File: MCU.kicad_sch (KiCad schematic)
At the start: 104 parts, among them J1 Conn_01x02_Pin, J11 Logger Connector, J12 UART Connector, J13 External UART, J14 External I2C, J15 JTAG Header, J2 Conn_01x02_Pin, J27 Conn_01x02_Pin, SW1 XRSn_button, U13 M24M01E-FMN6TP, U17 TRS3221EIPWR, U18 BZX84C3V3TS-7-F, U19 BZX84C3V3TS-7-F, U20 BZX84C3V3TS-7-F, U21 MIC920YC5-TR, U5 F280025PNS, Y2 H130B-16.000-18-3030-EXT-TR

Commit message: DONE! Added ESD protection & finalized everything before, this thing is ready for production
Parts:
- removed TP63, TP64, TP65, TP66: RCT-0C, digikey-footprints:PROBE_PAD_0805, symbol dk_Test-Points:RCT-0C
- added D10, D9: ESD8104MUTAG, ESD8104MUTAG:DIO_ESD8104MUTAG, symbol ESD8104MUTAG:ESD8104MUTAG
- added U22, U23: ESD7C3.3DT5G, SOT_C3.3DT5G_ONS, symbol ESD7C3-3DT5G:ESD7C3.3DT5G
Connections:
- net GND: now also D10.3 (GND), D10.8 (GND), D9.3 (GND), D9.8 (GND), U22.3, U23.3
- net I2CB_SCL: now also D10.4
- net I2CB_SDA: now also D10.5
- net JTAG_TCK: now also D9.5
- net JTAG_TDI: now also D9.1
- net JTAG_TDO: now also D9.4
- net JTAG_TMS: now also D9.2
- net LINB_RX: now also U23.2
- net LINB_TX: now also U23.1
- net MCU_IO_3V3: now also D10.2
- net RS232_RX: now also U22.1
- net RS232_TX: now also U22.2
- net XRSn: now also D10.1
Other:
- moved on the sheet: C111, C49, C50, C51, C52, C53, C54, C55, C56, C58, C59, C61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

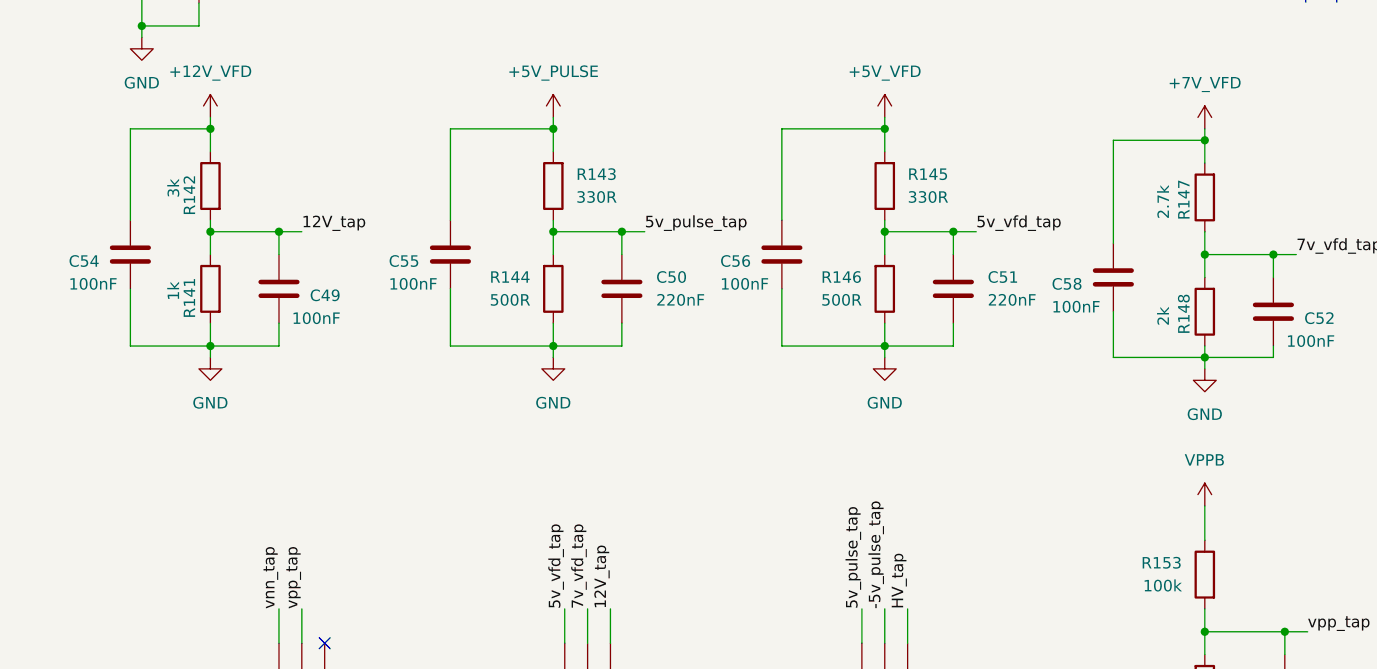
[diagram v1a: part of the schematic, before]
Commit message: edited voltage sensing resistor values to give headroom
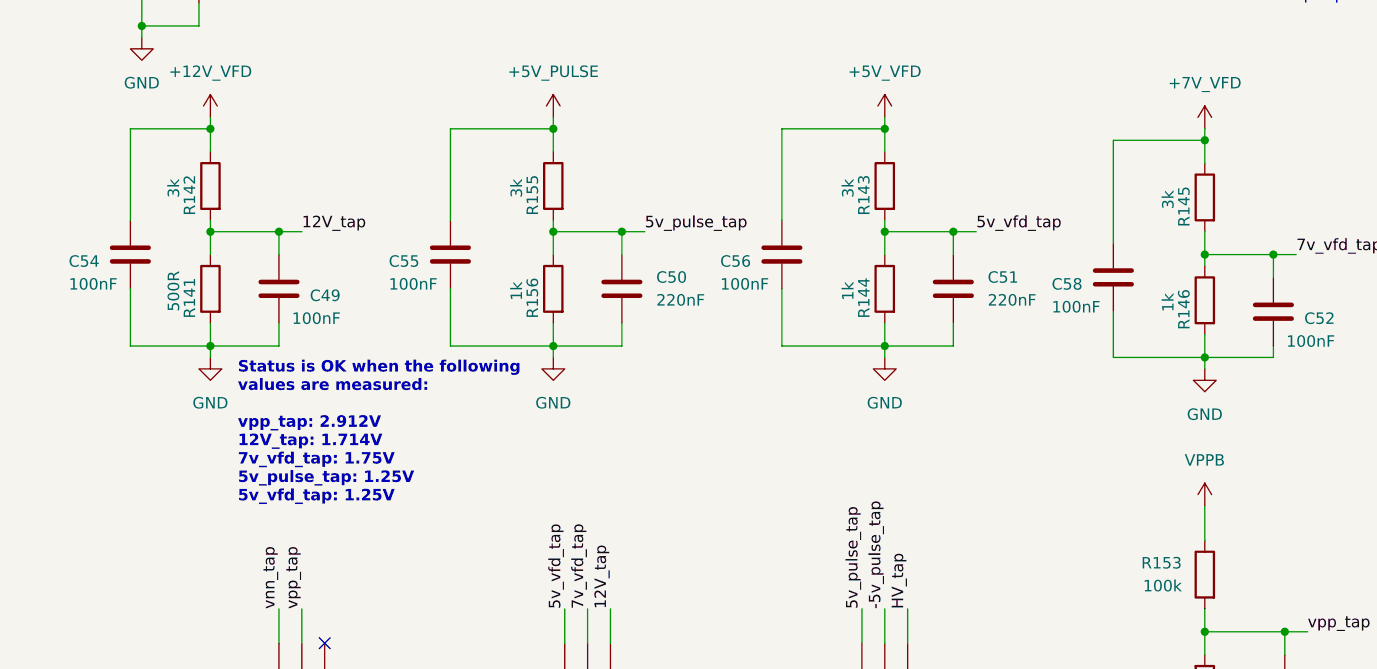
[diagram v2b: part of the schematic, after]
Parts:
- removed R147: 2.7k, Resistor_SMD:R_0603_1608Metric, symbol Device:R
- removed R148: 2k, Resistor_SMD:R_0603_1608Metric, symbol Device:R
- added R155: 3k, Resistor_SMD:R_0603_1608Metric, symbol Device:R
- added R156: 1k, Resistor_SMD:R_0603_1608Metric, symbol Device:R
- R141: value 1k -> 500R
- R143, R145: value 330R -> 3k
- R144, R146: value 500R -> 1k
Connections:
- net +5V_PULSE: now also R155.1; no longer R143.2
- net +5V_VFD: now also R143.1; no longer R145.2
- net +7V_VFD: now also R145.1
- net 5v_pulse_tap: now also R155.2, R156.1; no longer R143.1, R144.2
- net 5v_vfd_tap: now also R143.2, R144.1; no longer R145.1, R146.2
- net 7v_vfd_tap: now also R145.2, R146.1
- net GND: now also R144.2, R146.2, R156.2; no longer R144.1, R146.1
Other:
- note added: "Status is OK when the following values are measured: vpp_tap: 2.912V 12V_tap: 1.714V 7v_vfd_tap: 1.75V 5v_pulse_tap: 1.25V 5v_vfd_tap: 1.25V"

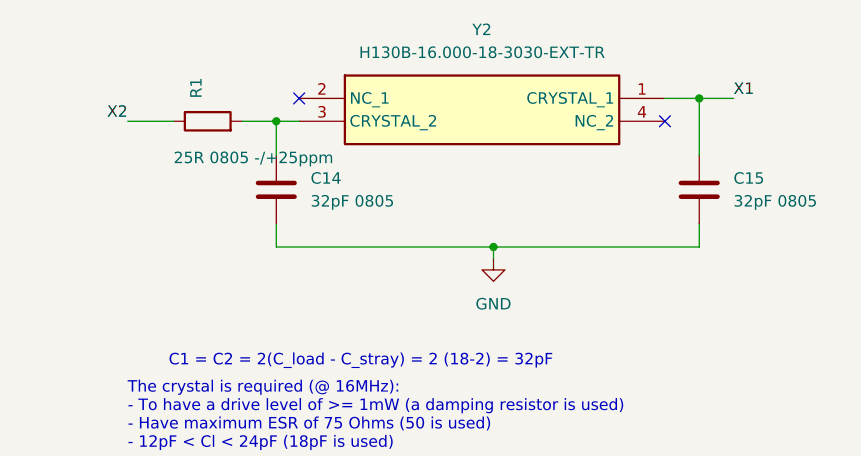
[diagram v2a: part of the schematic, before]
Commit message: Several finishing updates to fit stocks & changed SMA from SMD to THT, updated schematics too
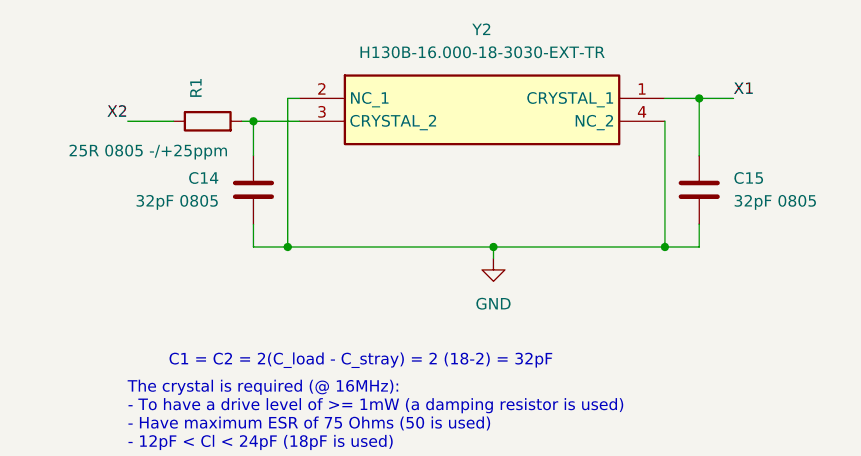
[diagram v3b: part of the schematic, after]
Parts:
- U22, U23: footprint SOT_C3.3DT5G_ONS -> ESD7C3-3DT5G:SOT_C3.3DT5G_ONS
- Y2: footprint KiCad:H130B16000183030EXTTR -> H130B-16.000-18-3030-EXT-TR:H130B16000183030EXTTR
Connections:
- net GND: now also Y2.2 (NC_1), Y2.4 (NC_2)
- no-connect marks 10 -> 8
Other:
- moved on the sheet: C14
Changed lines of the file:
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@@
 	)
 	(junction
-		(at 33.02 24.13)
+		(at 265.43 187.96)
 		(diameter 0)
 		(color 0 0 0 0)
 	)
 	(junction
-		(at 265.43 187.96)
+		(at 158.75 264.16)
 		(diameter 0)
 		(color 0 0 0 0)
 	)
 	(junction
-		(at 158.75 264.16)
+		(at 19.05 215.9)
 		(diameter 0)
 		(color 0 0 0 0)
 	)
 	(junction
-		(at 19.05 215.9)
+		(at 76.2 38.1)
 		(diameter 0)
 		(color 0 0 0 0)
@@
 	)
 	(junction
+		(at 30.48 24.13)
+		(diameter 0)
+		(color 0 0 0 0)
+	)
+	(junction
 		(at 19.05 85.09)
 		(diameter 0)
@@
 	)
 	(junction
+		(at 34.29 38.1)
+		(diameter 0)
+		(color 0 0 0 0)
+	)
+	(junction
 		(at 53.34 69.85)
 		(diameter 0)
@@
 	)
 	(no_connect
-		(at 76.2 24.13)
-	)
-	(no_connect
 		(at 85.09 215.9)
 	)
 	(no_connect
-		(at 35.56 21.59)
-	)
-	(no_connect
 		(at 179.07 124.46)
 	)
@@
 	(wire
 		(pts
-			(xy 33.02 38.1) (xy 57.15 38.1)
+			(xy 30.48 38.1) (xy 34.29 38.1)
 		)
 		(stroke
@@
 	(wire
 		(pts
+			(xy 76.2 38.1) (xy 80.01 38.1)
+		)
+		(stroke
+			(width 0)
+			(type default)
+		)
+	)
+	(wire
+		(pts
 			(xy 24.13 154.94) (xy 24.13 156.21)
 		)
@@
 	(wire
 		(pts
+			(xy 76.2 24.13) (xy 76.2 38.1)
+		)
+		(stroke
+			(width 0)
+			(type default)
+		)
+	)
+	(wire
+		(pts
 			(xy 119.38 132.08) (xy 143.51 132.08)
 		)
@@
 	(wire
 		(pts
+			(xy 30.48 24.13) (xy 35.56 24.13)
+		)
+		(stroke
+			(width 0)
+			(type default)
+		)
+	)
+	(wire
+		(pts
 			(xy 217.17 194.31) (xy 217.17 200.66)
 		)
@@
 	(wire
 		(pts
+			(xy 34.29 38.1) (xy 57.15 38.1)
+		)
+		(stroke
+			(width 0)
+			(type default)
+		)
+	)
+	(wire
+		(pts
 			(xy 52.07 156.21) (xy 52.07 158.75)
 		)
@@
 	(wire
 		(pts
-			(xy 57.15 38.1) (xy 80.01 38.1)
+			(xy 57.15 38.1) (xy 76.2 38.1)
 		)
 		(stroke
@@
 	(wire
 		(pts
-			(xy 33.02 35.56) (xy 33.02 38.1)
+			(xy 30.48 35.56) (xy 30.48 38.1)
 		)
 		(stroke
@@
 	(wire
 		(pts
-			(xy 29.21 24.13) (xy 33.02 24.13)
+			(xy 29.21 24.13) (xy 30.48 24.13)
 		)
 		(stroke
@@
 	(wire
 		(pts
+			(xy 34.29 21.59) (xy 34.29 38.1)
+		)
+		(stroke
+			(width 0)
+			(type default)
+		)
+	)
+	(wire
+		(pts
 			(xy 128.27 248.92) (xy 127 248.92)
 		)
@@
 	(wire
 		(pts
-			(xy 33.02 24.13) (xy 33.02 27.94)
+			(xy 30.48 24.13) (xy 30.48 27.94)
 		)
 		(stroke
@@
 	(wire
 		(pts
+			(xy 35.56 21.59) (xy 34.29 21.59)
+		)
+		(stroke
+			(width 0)
+			(type default)
+		)
+	)
+	(wire
+		(pts
 			(xy 121.92 160.02) (xy 121.92 162.56)
 		)
@@
 	(wire
 		(pts
-			(xy 35.56 24.13) (xy 33.02 24.13)
-		)
-		(stroke
-			(width 0)
-			(type default)
-		)
-	)
-	(wire
-		(pts
 			(xy 262.89 275.59) (xy 265.43 275.59)
 		)
@@
 			)
 		)
-		(property "Footprint" "SOT_C3.3DT5G_ONS"
+		(property "Footprint" "ESD7C3-3DT5G:SOT_C3.3DT5G_ONS"
 			(at 121.92 154.94 0)
 			(effects
@@
 		)
 		(property "Value" "25R 0805 -/+25ppm"
-			(at 39.37 28.194 90)
+			(at 27.686 27.432 90)
 			(effects
 				(font
@@
 			)
 		)
-		(property "Footprint" "KiCad:H130B16000183030EXTTR"
+		(property "Footprint" "H130B-16.000-18-3030-EXT-TR:H130B16000183030EXTTR"
 			(at 72.39 116.51 0)
 			(effects
@@
 	(symbol
 		(lib_id "Device:C")
-		(at 33.02 31.75 0)
+		(at 30.48 31.75 0)
+		(mirror y)
 		(unit 1)
 		(exclude_from_sim no)
@@
 		(on_board yes)
 		(dnp no)
-		(fields_autoplaced yes)
 		(property "Reference" "C14"
-			(at 36.83 30.4799 0)
+			(at 26.67 30.4799 0)
 			(effects
 				(font
@@
 		)
 		(property "Value" "32pF 0805"
-			(at 36.83 33.0199 0)
+			(at 26.67 33.0199 0)
 			(effects
 				(font
@@
 		)
 		(property "Footprint" "Capacitor_SMD:C_0603_1608Metric"
-			(at 33.9852 35.56 0)
+			(at 29.5148 35.56 0)
 			(effects
 				(font
@@
 		)
 		(property "Datasheet" "~"
-			(at 33.02 31.75 0)
+			(at 30.48 31.75 0)
 			(effects
 				(font
@@
 		)
 		(property "Description" "Unpolarized capacitor"
-			(at 33.02 31.75 0)
+			(at 30.48 31.75 0)
 			(effects
 				(font
@@
 			)
 		)
-		(property "Footprint" "SOT_C3.3DT5G_ONS"
+		(property "Footprint" "ESD7C3-3DT5G:SOT_C3.3DT5G_ONS"
 			(at 96.52 154.94 0)
 			(effects
